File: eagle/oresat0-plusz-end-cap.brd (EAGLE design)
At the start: 105.6 x 105.6 mm, 31 parts, among them U1 LTC4305, U2 MMC5883MA, U3 MMC5883MA

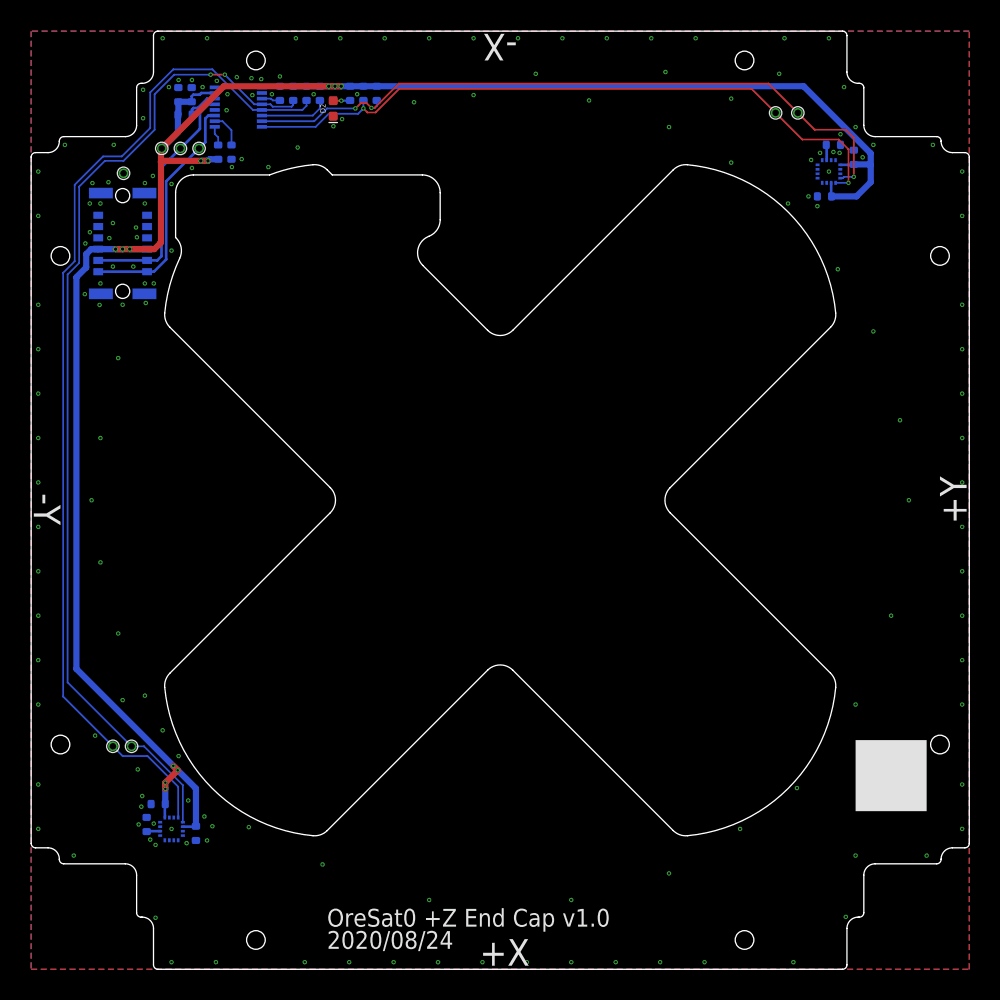
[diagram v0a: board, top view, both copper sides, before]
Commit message: Removed connector cutout from board outline. Increased restrict area for turnstile antenna. Changed some traces to the top layer to avoid the bstop area, and the new restrict area. Added NP resistors connecting magnetometer interrupts to i2c buffer alert inputs. Moved components away from backplane.
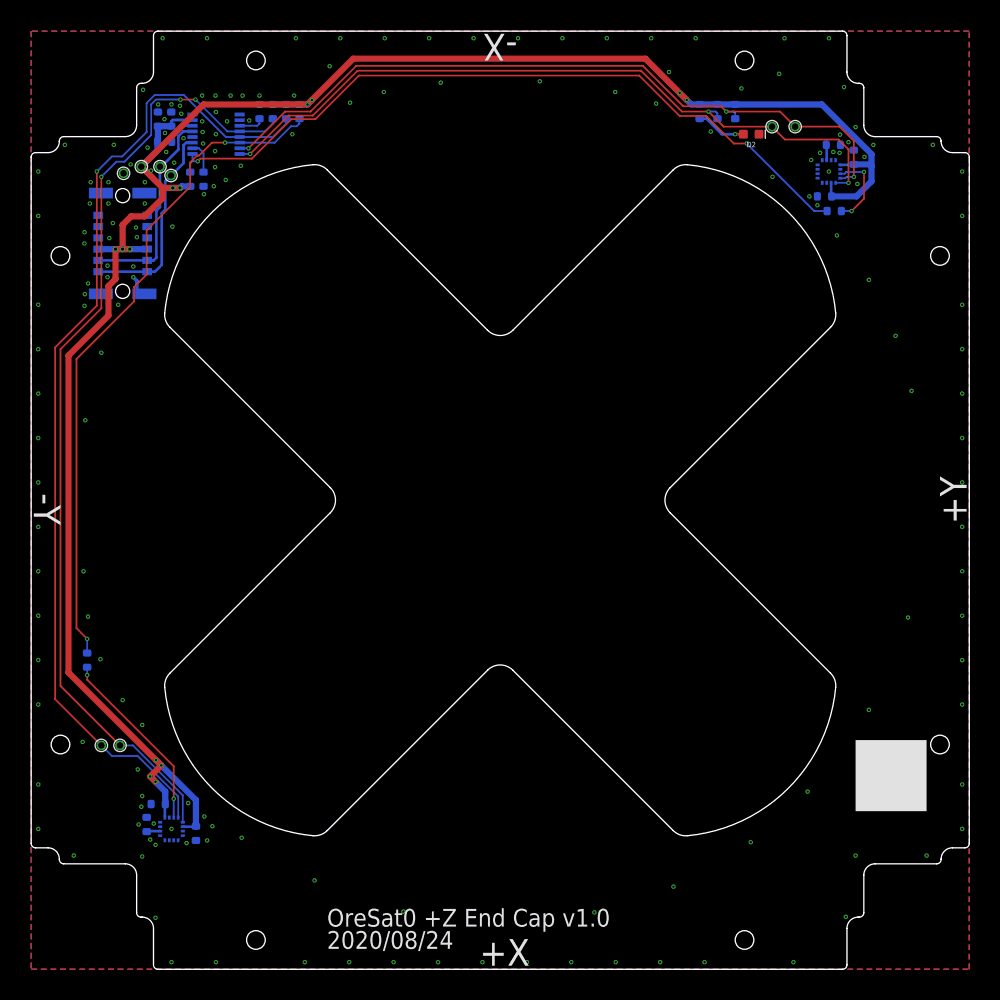
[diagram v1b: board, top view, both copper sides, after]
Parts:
- added R11, R12: 4.7k, oresat-rcl:.0603-B-NOSILK
- moved D2 47.1 mm to (81.0, 94.0), turned to 0 degrees
- moved R5 40.4 mm to (79.2, 96.5)
- moved R4 39.9 mm to (77.2, 96.5)
- moved R2 39.4 mm to (75.2, 96.5)
- moved TP6 4.38 mm to (15.8, 89.3)
- moved R1 4.38 mm to (19.4, 88.9)
- moved R8 4.38 mm to (17.9, 88.9)
- moved U1 3.94 mm to (20.8, 94.0)
- moved R10 3.82 mm to (15.0, 93.2)
- moved C3 3.59 mm to (15.8, 95.7)
- moved C4 3.59 mm to (14.3, 95.7)
- moved TP3 3.08 mm to (14.5, 90.3)
- moved TP7 3.08 mm to (12.4, 90.3)
- moved R3 3.08 mm to (30.2, 96.5)
- moved R6 3.08 mm to (28.7, 96.5)
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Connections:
- new net N$10: R12.1, U2.15
- new net N$7: R11.1, U3.15
- net N$4: now also R11.2
- net N$6: now also R12.2
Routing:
- net N$6: track 2.21 -> 83.9 mm, vias 0 -> 2
- net N$4: track 7.76 -> 75.7 mm, vias 0 -> 2
- net N$7: track 0.00 -> 21.0 mm, vias 0 -> 2
- net N$10: track 0.00 -> 8.88 mm, vias 0 -> 2
- net SCL2: track 77.1 -> 83.0 mm, vias 2 -> 3
- net SDA2: track 78.6 -> 83.8 mm
- net I2C-SDA: track 27.1 -> 23.1 mm
- net I2C-SCL: track 27.3 -> 23.3 mm
- net N$271: track 1.92 -> 5.65 mm
- net SCL1: track 112.0 -> 108.4 mm, vias 2 -> 3
- net SDA1: track 115.3 -> 112.0 mm, vias 0 -> 1
- net 3.3V: track 225.2 -> 228.2 mm, vias 12 -> 13
- net GND: track 0.00 -> 2.84 mm, vias 169 -> 178
- net N$1: track 2.11 -> 2.88 mm
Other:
- outline, holes or cut-outs redrawn

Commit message: v1.0 end caps for OreSat0!
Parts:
- R11, R12: value 4.7k -> NP
- U1: value LTC4305 -> LTC4305IGN
- moved R11 0.70 mm to (7.00, 34.8)
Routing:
- net GND: track 2.84 -> 5.54 mm, vias 178 -> 177
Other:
- outline, holes or cut-outs redrawn
- board text added: "2020/08/28"
- board text added: "OreSat0"
- board text added: "Oregon's First Satellite!"
- board text removed: "2020/08/24"
